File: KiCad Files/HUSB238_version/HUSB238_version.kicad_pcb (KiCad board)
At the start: 2 copper layers, 54 x 12.9 mm, 33 parts, among them J2 2.54_PinHeader_02x02_SMD, J3 2.54_PinHeader_02x02_SMD, J4 2.5P Terminal Block, J9 USB_C_USB2.0_14P, Q2 AONR21307, Q9 AO3400A, SW1 SW_DIP_x05, U1 LM317L_SOT-89, U3 HUSB238_USB_PD, U4 USBLC6-2SC6

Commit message: changed pcb
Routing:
- net Net-(R15-Pad2): track 0.00 -> 7.93 mm
- net Net-(R17-Pad2): track 0.00 -> 5.67 mm
- net Net-(R16-Pad2): track 0.00 -> 5.33 mm
- net Net-(R18-Pad2): track 0.00 -> 2.06 mm
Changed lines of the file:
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@@
-		)
-	)
-	(dimension
-		(type orthogonal)
-		(layer "Dwgs.User")
-		(pts
-			(xy 193.07 116.87) (xy 140.37 116.58)
-		)
-		(height 6.67)
-		(orientation 0)
-		(format
-			(prefix "")
-			(suffix "")
-			(units 3)
-			(units_format 0)
-			(precision 4)
-			(suppress_zeroes yes)
-		)
-		(style
-			(thickness 0.1)
-			(arrow_length 1.27)
-			(text_position_mode 0)
-			(arrow_direction outward)
-			(extension_height 0.58642)
-			(extension_offset 0.5)
-			(keep_text_aligned yes)
-		)
-		(gr_text "52.7"
-			(at 166.72 122.39 0)
-			(layer "Dwgs.User")
-			(effects
-				(font
-					(size 1 1)
-					(thickness 0.15)
-				)
-			)
 		)
 	)
@@
 	)
 	(segment
+		(start 150.34384 110.76)
+		(end 151.29484 111.711)
+		(width 0.2)
+		(layer "F.Cu")
+		(net 13)
+	)
+	(segment
+		(start 155.399 111.711)
+		(end 156.92 110.19)
+		(width 0.2)
+		(layer "F.Cu")
+		(net 13)
+	)
+	(segment
+		(start 150.0175 110.76)
+		(end 150.34384 110.76)
+		(width 0.2)
+		(layer "F.Cu")
+		(net 13)
+	)
+	(segment
+		(start 151.29484 111.711)
+		(end 155.399 111.711)
+		(width 0.2)
+		(layer "F.Cu")
+		(net 13)
+	)
+	(segment
+		(start 150.856 108.669)
+		(end 150.025 109.5)
+		(width 0.2)
+		(layer "F.Cu")
+		(net 14)
+	)
+	(segment
+		(start 152.859 108.669)
+		(end 150.856 108.669)
+		(width 0.2)
+		(layer "F.Cu")
+		(net 14)
+	)
+	(segment
+		(start 154.38 110.19)
+		(end 152.859 108.669)
+		(width 0.2)
+		(layer "F.Cu")
+		(net 14)
+	)
+	(segment
+		(start 162.589 111.711)
+		(end 163.2825 111.0175)
+		(width 0.2)
+		(layer "F.Cu")
+		(net 15)
+	)
+	(segment
+		(start 160.981 111.711)
+		(end 162.589 111.711)
+		(width 0.2)
+		(layer "F.Cu")
+		(net 15)
+	)
+	(segment
+		(start 163.2825 111.0175)
+		(end 163.2825 110.09)
+		(width 0.2)
+		(layer "F.Cu")
+		(net 15)
+	)
+	(segment
+		(start 159.46 110.19)
+		(end 160.981 111.711)
+		(width 0.2)
+		(layer "F.Cu")
+		(net 15)
+	)
+	(segment
+		(start 162 110.19)
+		(end 162 109.975)
+		(width 0.2)
+		(layer "F.Cu")
+		(net 16)
+	)
+	(segment
+		(start 162 109.975)
+		(end 163.305 108.67)
+		(width 0.2)
+		(layer "F.Cu")
+		(net 16)
+	)
+	(segment

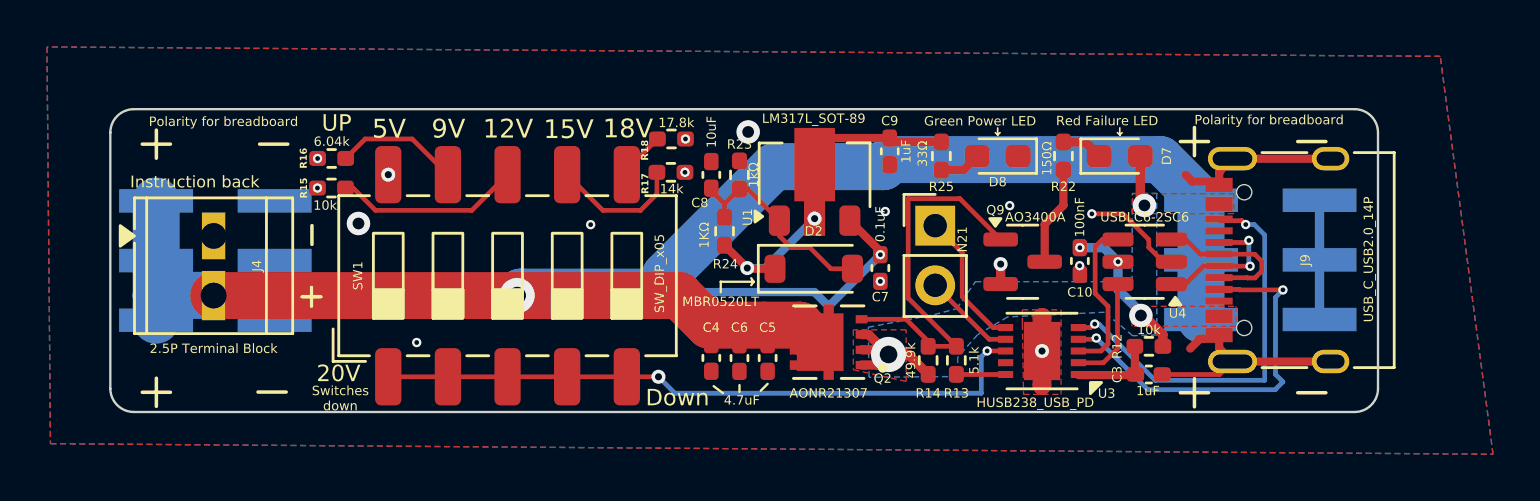
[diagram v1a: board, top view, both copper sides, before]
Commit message: many changes and new pcb design. Also updated husb238 design after boards arraived
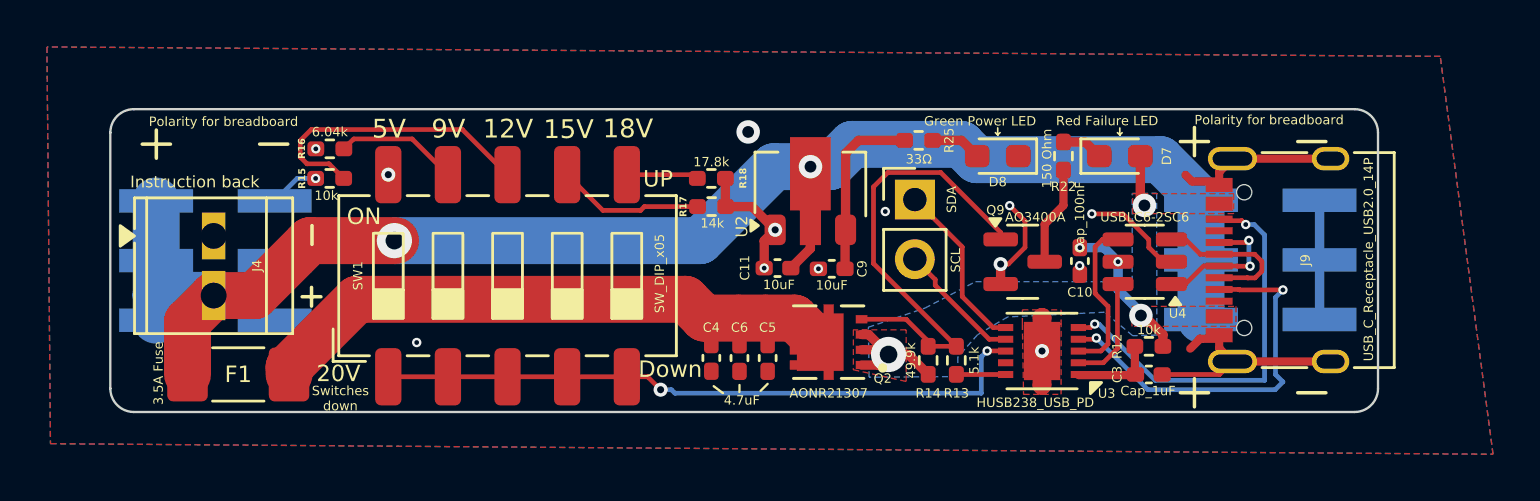
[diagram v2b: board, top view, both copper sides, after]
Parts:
- removed C7: 0.1uF, Capacitor_SMD:C_0402_1005Metric_Pad0.74x0.62mm_HandSolder
- removed C8: 10uF, Capacitor_SMD:C_0402_1005Metric_Pad0.74x0.62mm_HandSolder
- removed D2: MBR0520LT, Diode_SMD:D_SOD-123
- removed R23: 1kΩ, Resistor_SMD:R_0402_1005Metric_Pad0.72x0.64mm_HandSolder
- removed R24: 1KΩ, Resistor_SMD:R_0402_1005Metric_Pad0.72x0.64mm_HandSolder
- removed U1: LM317L_SOT-89, Package_TO_SOT_SMD:SOT-89-3
- added C11: 10uF, Capacitor_SMD:C_0402_1005Metric_Pad0.74x0.62mm_HandSolder, F.Cu at (168.4, 114.2)
- added F1: Fuse_3.5A, Capacitor_SMD:C_1808_4520Metric_Pad1.72x2.30mm_HandSolder, F.Cu at (145.4, 118.7)
- added U2: HT75xx-1-SOT89, Package_TO_SOT_SMD:SOT-89-3, F.Cu at (169.8, 110.6)
- C10: value 100nF -> Cap_100nF
- C3: value 1uF -> Cap_1uF
- C9: value 1uF -> 10uF
- J2, J3: value 2.54_PinHeader_02x02_SMD -> Conn_02x02_Counter_Clockwise
- J4: value 2.5P Terminal Block -> Conn_01x02_Pin
- J9: value USB_C_USB2.0_14P -> USB_C_Receptacle_USB2.0_14P
- R22: value 150Ω -> 150 Ohm
- moved C9 5.58 mm to (170.7, 114.2), turned to 180 degrees
- moved R18 2.39 mm to (165.6, 110.3)
- moved R17 2.27 mm to (165.6, 111.5)
- moved N21 1.41 mm to (174.3, 111.2)
- moved R25 1.18 mm to (174.4, 108.7), turned to 180 degrees
- moved R15 0.42 mm to (149.3, 110.3)
- moved R16 0.42 mm to (149.3, 109.1)
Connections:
- C4 pad 2: VCC -> Net-(C4-Pad2)
- C5 pad 2: VCC -> Net-(C4-Pad2)
- C6 pad 2: VCC -> Net-(C4-Pad2)
- Q2 pad 5_6_7_8: VCC -> Net-(C4-Pad2)
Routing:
- net Net-(C4-Pad2): track 0.00 -> 28.4 mm
- net VCC: track 86.6 -> 64.1 mm
- net GND: track 31.1 -> 42.2 mm, vias 16 -> 14
- net Net-(D2-A): track 8.97 -> 0.00 mm
- net Net-(U2-VOUT): track 14.9 -> 7.67 mm, vias 2 -> 0
- net Net-(R15-Pad2): track 7.93 -> 12.7 mm
- net Net-(Q9-G): track 16.4 -> 19.9 mm
- net SCL 1: track 3.95 -> 5.42 mm
- net SDA 1: track 5.90 -> 7.37 mm
- net Net-(R18-Pad2): track 2.06 -> 3.07 mm
- net Net-(R17-Pad2): track 5.67 -> 6.25 mm
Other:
- board text added: "3.5A Fuse"
- board text added: "Added 1808 replacable Fuse. Max output current is 3.25A"
- board text added: "ON"
- board text added: "SCL"
- board text added: "SDA"
